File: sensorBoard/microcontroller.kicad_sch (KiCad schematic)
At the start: 14 parts, among them U1 STM32L476RGTx, Y1 8MHz

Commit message: added the footprints, connectors left
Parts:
- C10, C11, C12, C3, C5, C6, C7, C8, C9: footprint (none) -> Capacitor_SMD:C_0805_2012Metric
- R13, R14, R6: footprint (none) -> Resistor_SMD:R_0805_2012Metric
- Y1: footprint (none) -> Crystal:Crystal_SMD_HC49-SD_HandSoldering
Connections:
- no-connect marks 1 -> 32
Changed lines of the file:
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@@
+	)
+	(no_connect
+		(at 147.32 101.6)
 	)
 	(no_connect
 		(at 124.46 40.64)
+	)
+	(no_connect
+		(at 147.32 48.26)
+	)
+	(no_connect
+		(at 111.76 88.9)
+	)
+	(no_connect
+		(at 147.32 114.3)
+	)
+	(no_connect
+		(at 147.32 71.12)
+	)
+	(no_connect
+		(at 147.32 111.76)
+	)
+	(no_connect
+		(at 147.32 124.46)
+	)
+	(no_connect
+		(at 147.32 116.84)
+	)
+	(no_connect
+		(at 147.32 96.52)
+	)
+	(no_connect
+		(at 147.32 109.22)
+	)
+	(no_connect
+		(at 147.32 66.04)
+	)
+	(no_connect
+		(at 111.76 99.06)
+	)
+	(no_connect
+		(at 111.76 86.36)
+	)
+	(no_connect
+		(at 111.76 81.28)
+	)
+	(no_connect
+		(at 111.76 96.52)
+	)
+	(no_connect
+		(at 111.76 63.5)
+	)
+	(no_connect
+		(at 147.32 119.38)
+	)
+	(no_connect
+		(at 147.32 121.92)
+	)
+	(no_connect
+		(at 111.76 83.82)
+	)
+	(no_connect
+		(at 147.32 127)
+	)
+	(no_connect
+		(at 111.76 91.44)
+	)
+	(no_connect
+		(at 111.76 73.66)
+	)
+	(no_connect
+		(at 111.76 93.98)
+	)
+	(no_connect
+		(at 147.32 93.98)
+	)
+	(no_connect
+		(at 111.76 78.74)
+	)
+	(no_connect
+		(at 147.32 68.58)
+	)
+	(no_connect
+		(at 147.32 83.82)
+	)
+	(no_connect
+		(at 111.76 71.12)
+	)
+	(no_connect
+		(at 111.76 104.14)
+	)
+	(no_connect
+		(at 147.32 55.88)
+	)
+	(no_connect
+		(at 147.32 58.42)
 	)
 	(wire
@@
 			)
 		)
-		(property "Footprint" ""
+		(property "Footprint" "Capacitor_SMD:C_0805_2012Metric"
 			(at 85.09 69.85 0)
 			(effects
@@
 			)
 		)
-		(property "Footprint" ""
+		(property "Footprint" "Capacitor_SMD:C_0805_2012Metric"
 			(at 153.67 31.75 0)
 			(effects
@@
 			)
 		)
-		(property "Footprint" ""
+		(property "Footprint" "Capacitor_SMD:C_0805_2012Metric"
 			(at 55.88 57.15 0)
 			(effects
@@
 			)
 		)
-		(property "Footprint" ""
+		(property "Footprint" "Capacitor_SMD:C_0805_2012Metric"
 			(at 173.99 31.75 0)
 			(effects
@@
 			)
 		)
-		(property "Footprint" ""
+		(property "Footprint" "Capacitor_SMD:C_0805_2012Metric"
 			(at 143.51 31.75 0)
 			(effects
@@
 			)
 		)
-		(property "Footprint" ""
+		(property "Footprint" "Capacitor_SMD:C_0805_2012Metric"
 			(at 194.31 31.75 0)
 			(effects
@@
 			)
 		)
-		(property "Footprint" ""
+		(property "Footprint" "Capacitor_SMD:C_0805_2012Metric"
 			(at 184.15 31.75 0)
 			(effects
@@
 			)
 		)
-		(property "Footprint" ""
+		(property "Footprint" "Resistor_SMD:R_0805_2012Metric"
 			(at 66.04 57.15 0)
 			(effects
@@
 			)
 		)
-		(property "Footprint" ""
+		(property "Footprint" "Resistor_SMD:R_0805_2012Metric"
 			(at 176.53 99.06 0)
 			(effects
@@
 			)
 		)
-		(property "Footprint" ""
+		(property "Footprint" "Crystal:Crystal_SMD_HC49-SD_HandSoldering"
 			(at 81.28 64.77 0)
 			(effects
@@
 			)
 		)
-		(property "Footprint" ""
+		(property "Footprint" "Capacitor_SMD:C_0805_2012Metric"
 			(at 77.47 69.85 0)
 			(effects
@@
 			)
 		)
-		(property "Footprint" ""
+		(property "Footprint" "Resistor_SMD:R_0805_2012Metric"
 			(at 168.91 99.06 0)
 			(effects
@@
 			)
 		)
-		(property "Footprint" ""
+		(property "Footprint" "Capacitor_SMD:C_0805_2012Metric"
 			(at 163.83 31.75 0)
 			(effects

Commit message: started the layout
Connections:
- net POLE_1_EN: no longer names the net of U1.22 (PA6)
- net POLE_2_EN: no longer names the net of U1.23 (PA7)
- no-connect marks 32 -> 34
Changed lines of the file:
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@@
+	)
+	(no_connect
+		(at 147.32 60.96)
 	)
 	(no_connect
@@
 	)
 	(no_connect
+		(at 147.32 63.5)
+	)
+	(no_connect
 		(at 111.76 96.52)
 	)
@@
 	(wire
 		(pts
-			(xy 147.32 60.96) (xy 161.29 60.96)
-		)
-		(stroke
-			(width 0)
-			(type default)
-		)
-	)
-	(wire
-		(pts
 			(xy 147.32 104.14) (xy 168.91 104.14)
 		)
@@
 		(pts
 			(xy 176.53 101.6) (xy 176.53 106.68)
-		)
-		(stroke
-			(width 0)
-			(type default)
-		)
-	)
-	(wire
-		(pts
-			(xy 147.32 63.5) (xy 161.29 63.5)
 		)
 		(stroke
@@
 		)
 	)
-	(hierarchical_label "POLE_1_EN"
-		(shape output)
-		(at 161.29 60.96 0)
-		(fields_autoplaced yes)
-		(effects
-			(font
-				(size 1.27 1.27)
-			)
-			(justify left)
-		)
-	)
 	(hierarchical_label "DIN"
 		(shape output)
@@
 		(fields_autoplaced yes)
 		(effects
-			(font
-				(size 1.27 1.27)
-			)
-			(justify left)
-		)
-	)
-	(hierarchical_label "POLE_2_EN"
-		(shape output)
-		(at 161.29 63.5 0)
-		(fields_autoplaced yes)
-		(effects

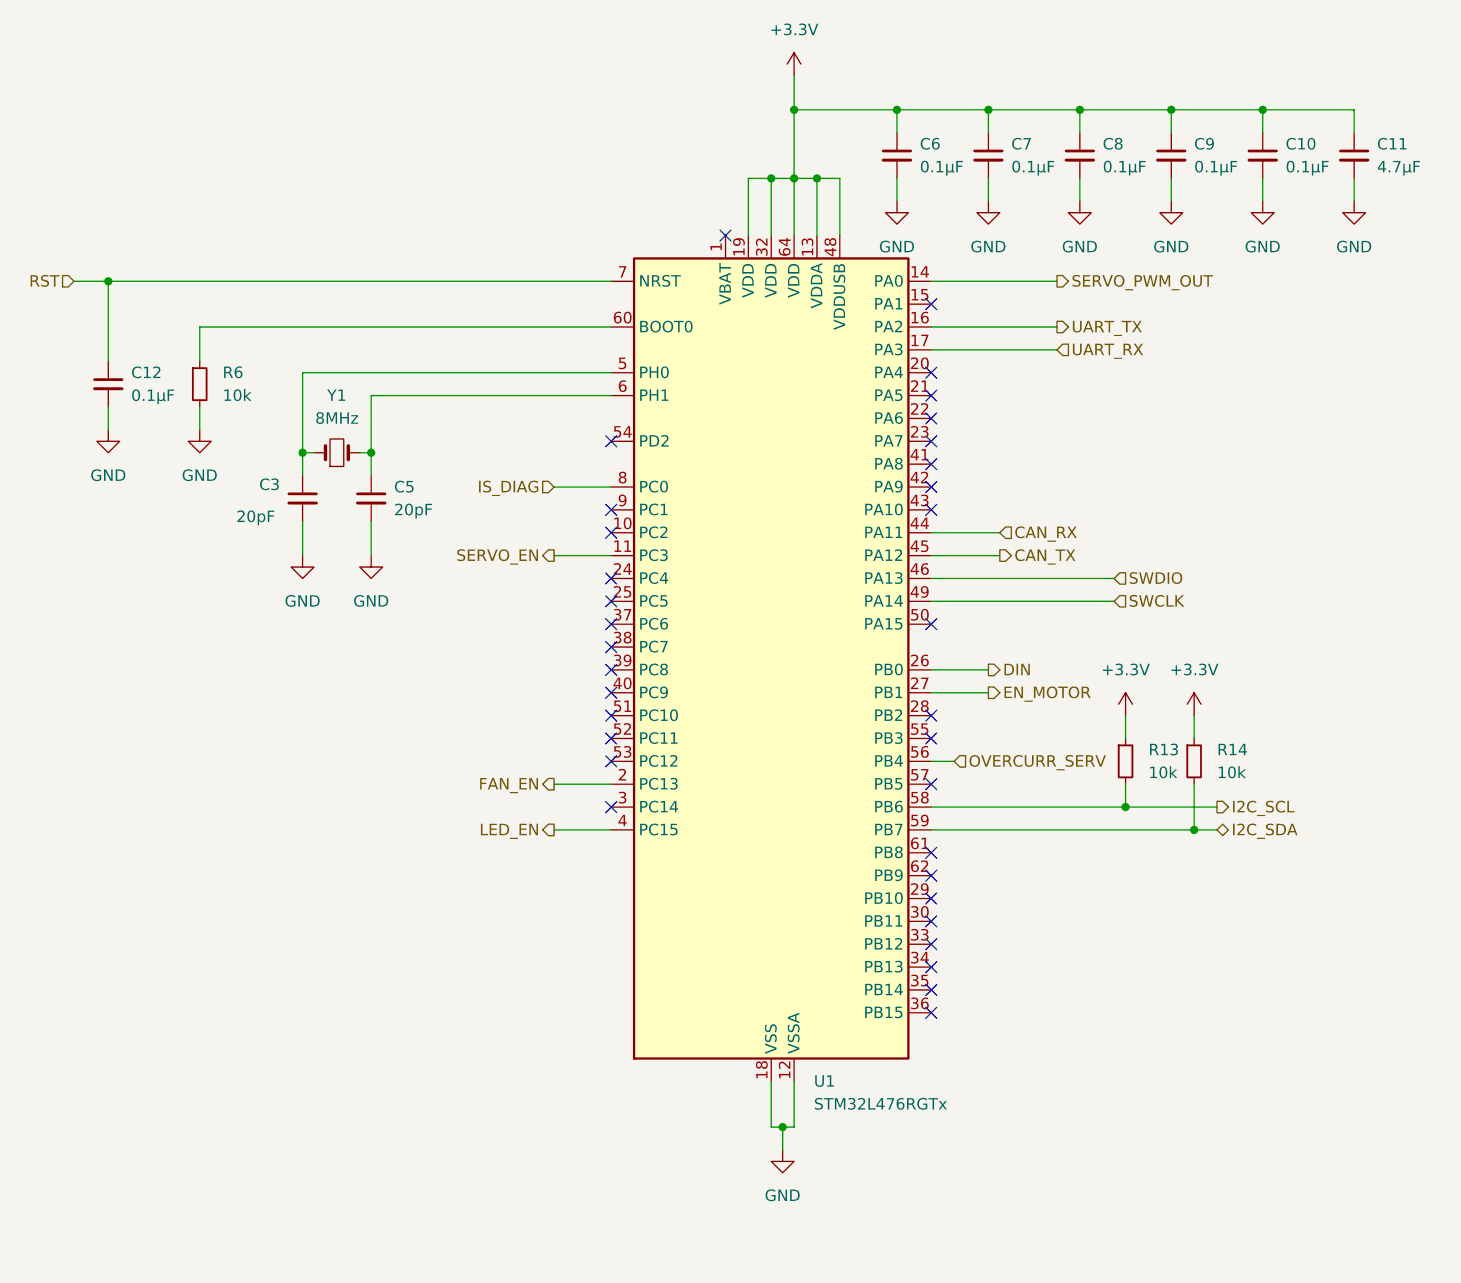
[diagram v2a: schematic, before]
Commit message: new two separate pcbs
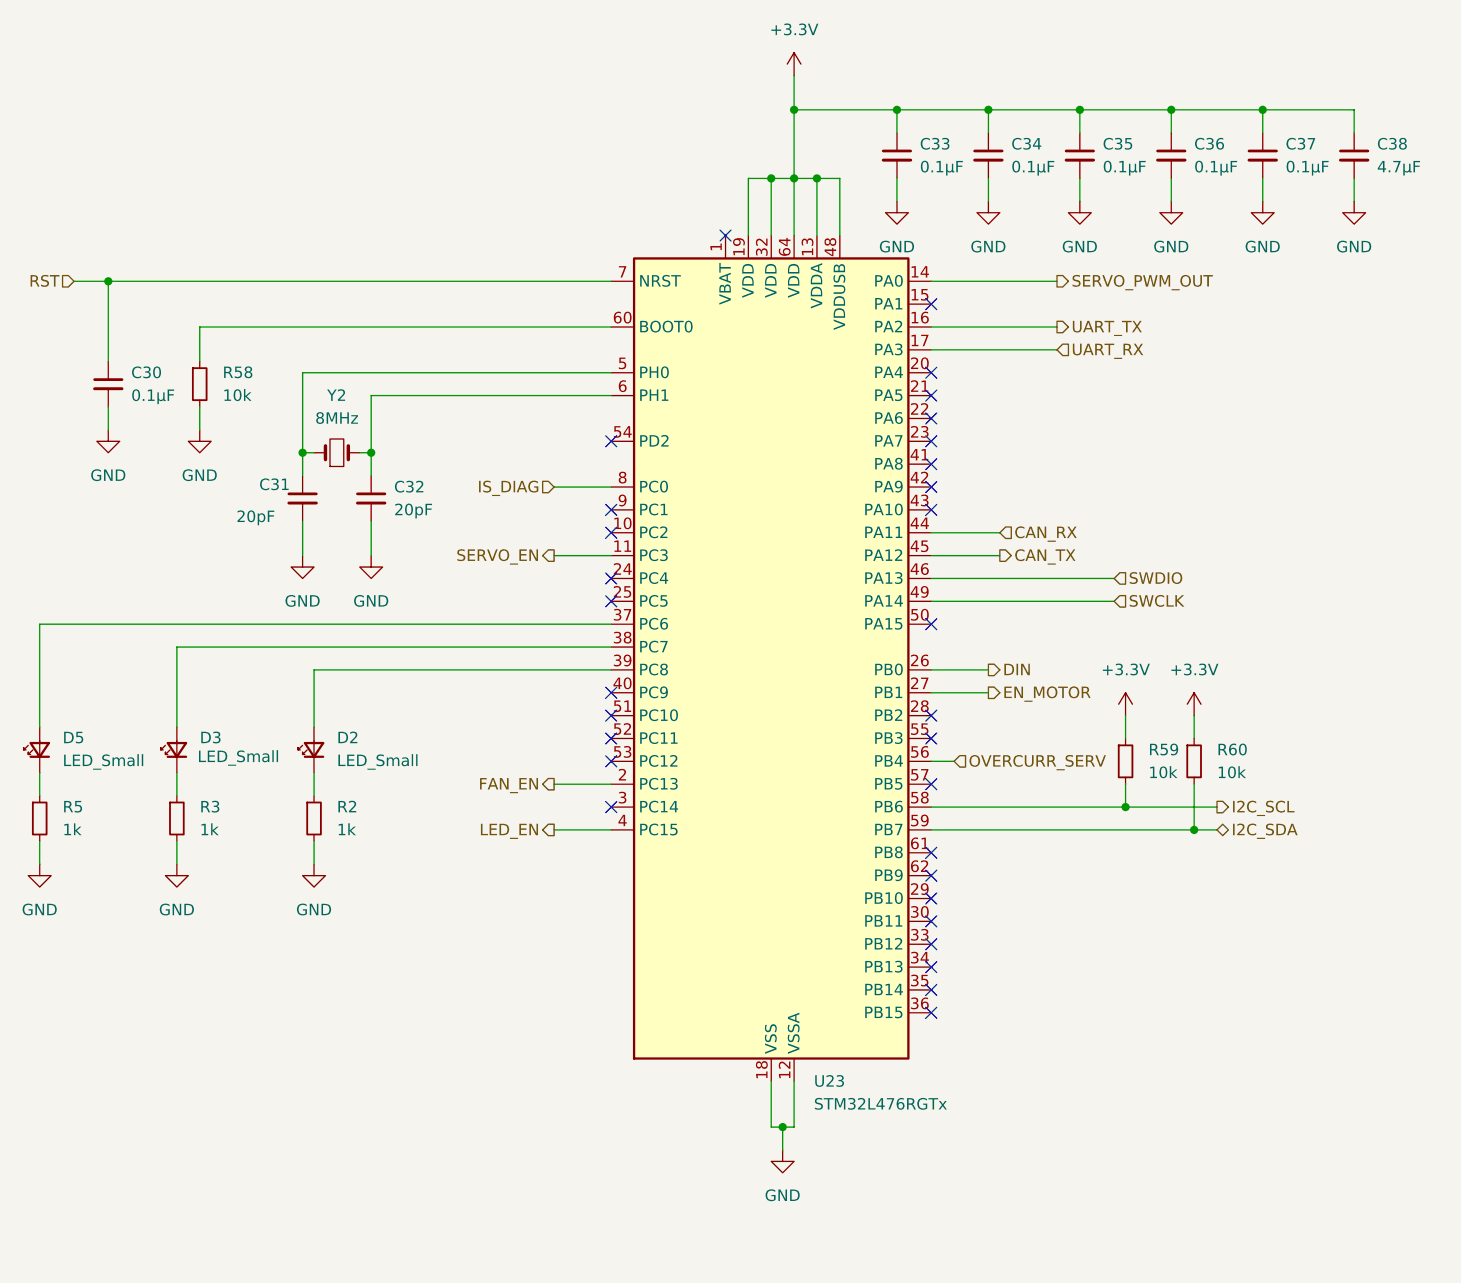
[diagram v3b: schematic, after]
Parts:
- added D2, D3, D5: LED_Small, LED_SMD:LED_0805_2012Metric, symbol Device:LED_Small
- added R2, R3, R5: 1k, Resistor_SMD:R_0805_2012Metric, symbol Device:R_Small
- renumbered C12 to C30, C3 to C31, C5 to C32, C6 to C33, C7 to C34, C8 to C35, C9 to C36, C10 to C37, C11 to C38, R6 to R58, R13 to R59, R14 to R60, U1 to U23, Y1 to Y2
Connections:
- net GND: now also R2.2, R3.2, R5.2
- net at U23.37 (PC6): now also D5.2 (A)
- net at U23.38 (PC7): now also D3.2 (A)
- net at U23.39 (PC8): now also D2.2 (A)
- new net: D2.1 (K), R2.1
- new net: D5.1 (K), R5.1
- new net: D3.1 (K), R3.1
- no-connect marks 34 -> 31
